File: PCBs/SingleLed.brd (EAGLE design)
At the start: 14.5 x 42 mm, 4 parts

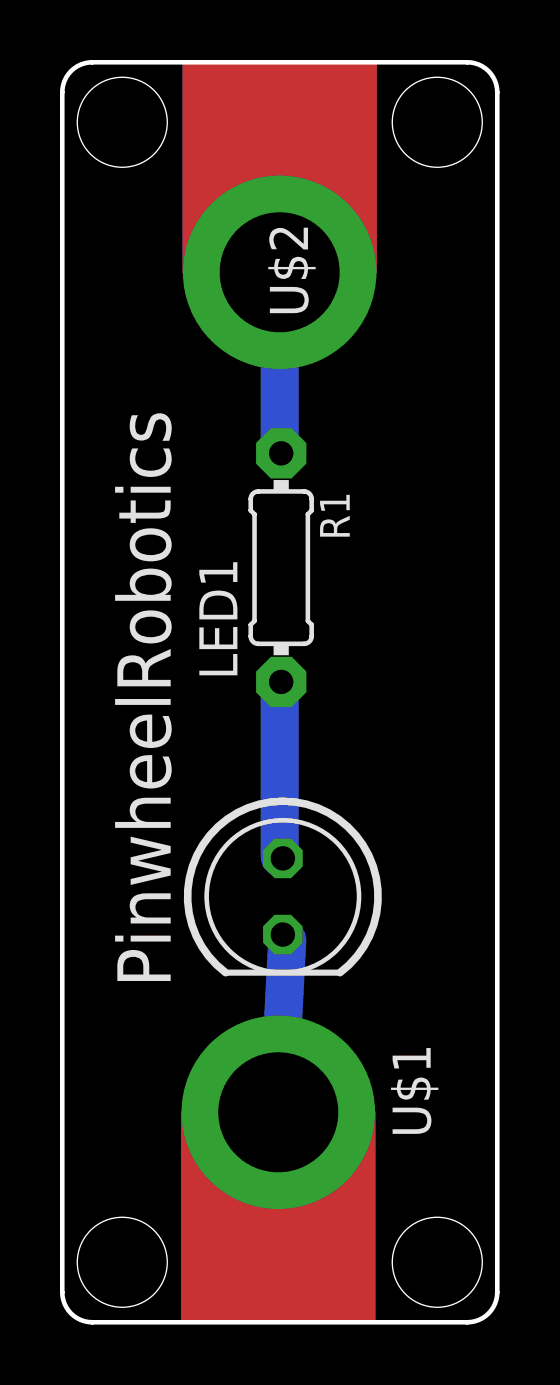
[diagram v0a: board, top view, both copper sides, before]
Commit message: Corrected dimesnion for
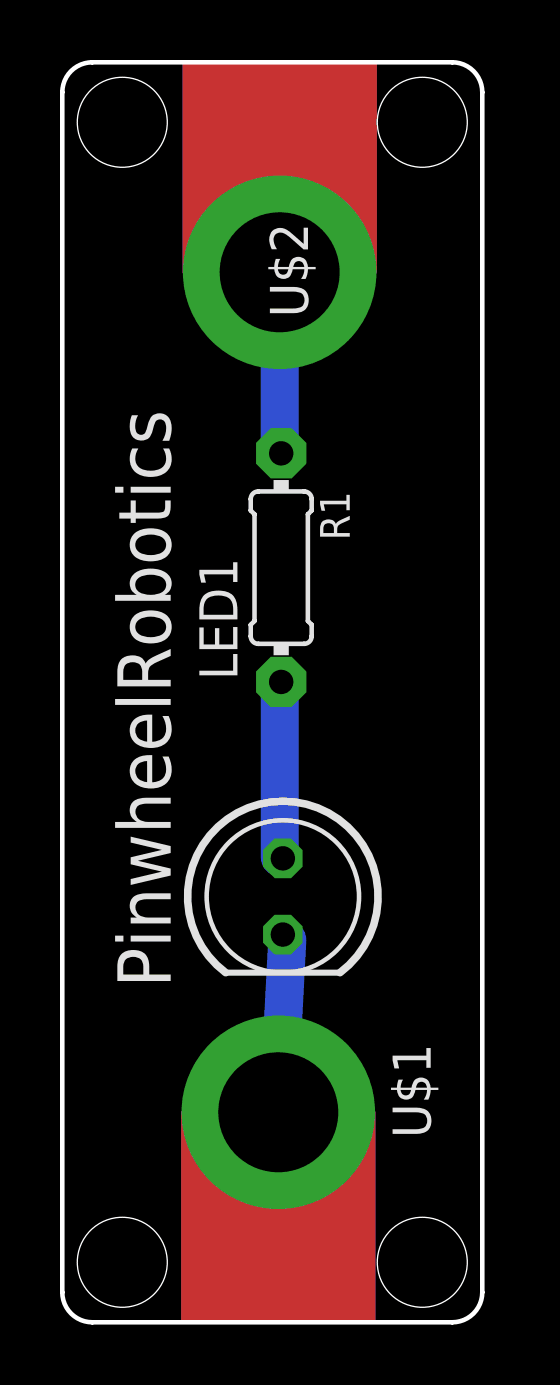
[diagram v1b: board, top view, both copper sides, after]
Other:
- board size 14.5 x 42 mm -> 14 x 42 mm
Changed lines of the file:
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@@
 <hole x="2" y="40" drill="3"/>
 <hole x="2" y="2" drill="3"/>
-<hole x="12.5" y="2" drill="3"/>
-<hole x="12.5" y="40" drill="3"/>
+<hole x="12" y="2" drill="3"/>
+<hole x="12" y="40" drill="3"/>
 <text x="3.613" y="11.161" size="1.778" layer="21" rot="R90">PinwheelRobotics</text>
 <text x="13.242" y="30.965" size="1.778" layer="22" rot="MR270">care@pinwheel.in</text>
-<wire x1="1" y1="0" x2="13.5" y2="0" width="0.1524" layer="20"/>
-<wire x1="13.5" y1="0" x2="14.5" y2="1" width="0.1524" layer="20" curve="90"/>
-<wire x1="14.5" y1="1" x2="14.5" y2="41" width="0.1524" layer="20"/>
-<wire x1="14.5" y1="41" x2="13.5" y2="42" width="0.1524" layer="20" curve="90"/>
-<wire x1="13.5" y1="42" x2="1" y2="42" width="0.1524" layer="20"/>
+<wire x1="1" y1="0" x2="13" y2="0" width="0.1524" layer="20"/>
+<wire x1="13" y1="0" x2="14" y2="1" width="0.1524" layer="20" curve="90"/>
+<wire x1="14" y1="1" x2="14" y2="41" width="0.1524" layer="20"/>
+<wire x1="14" y1="41" x2="13" y2="42" width="0.1524" layer="20" curve="90"/>
+<wire x1="13" y1="42" x2="1" y2="42" width="0.1524" layer="20"/>
 <wire x1="1" y1="42" x2="0" y2="41" width="0.1524" layer="20" curve="90"/>
 <wire x1="0" y1="41" x2="0" y2="1" width="0.1524" layer="20"/>
 <wire x1="0" y1="1" x2="1" y2="0" width="0.1524" layer="20" curve="90"/>
 <dimension x1="-2" y1="42" x2="-2" y2="0" x3="-3" y3="21" textsize="1.778" layer="1"/>
-<dimension x1="0" y1="42.5" x2="14.5" y2="42.5" x3="7.25" y3="44" textsize="1.778" layer="1"/>
+<dimension x1="13.5" y1="40" x2="13.5" y2="2" x3="20.5" y3="21" textsize="1.778" layer="1" dtype="diameter"/>
+<dimension x1="0" y1="43.5" x2="14" y2="43.5" x3="7" y3="45" textsize="1.778" layer="1"/>
+<dimension x1="2" y1="37.5" x2="12" y2="37.5" x3="7" y3="48.5" textsize="1.778" layer="1"/>
 </plain>
 <attributes>

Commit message: Update for Dim width is 42 length is 28 for type 2 pcb
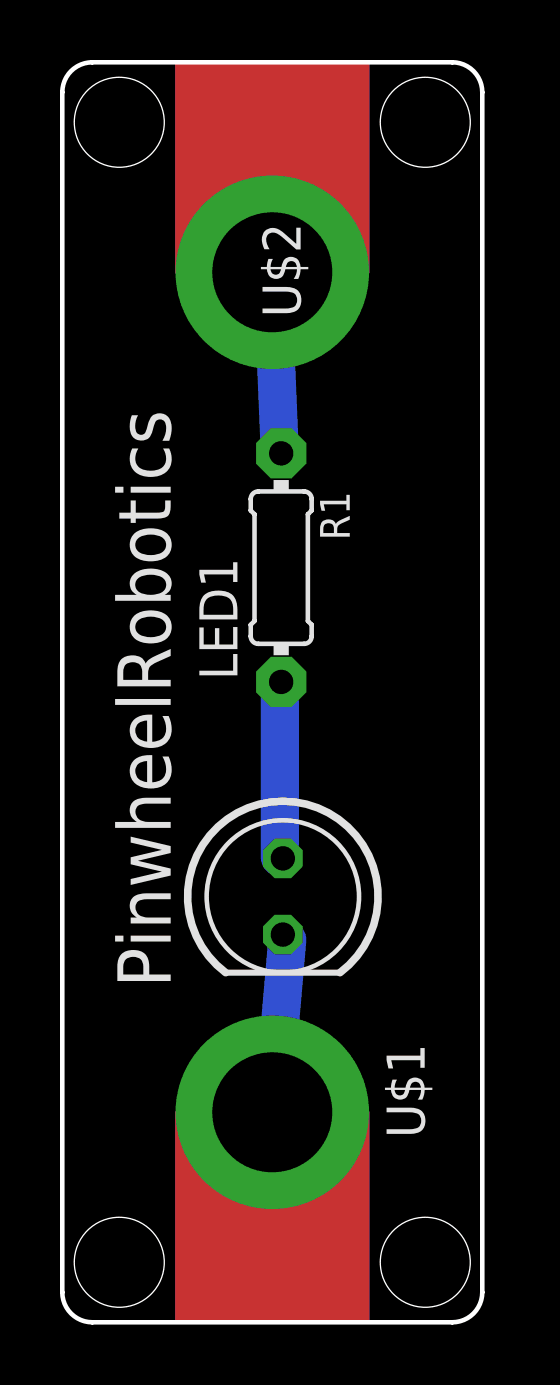
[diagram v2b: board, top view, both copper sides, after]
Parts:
- moved U$2 0.25 mm to (7.00, 35.0)
- moved U$1 0.20 mm to (7.00, 7.00)
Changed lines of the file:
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@@
 <drawing>
 <settings>
-<setting alwaysvectorfont="no"/>
+<setting alwaysvectorfont="yes"/>
 <setting verticaltext="up"/>
 </settings>
@@
 <board>
 <plain>
-<hole x="2" y="40" drill="3"/>
-<hole x="2" y="2" drill="3"/>
-<hole x="12" y="2" drill="3"/>
-<hole x="12" y="40" drill="3"/>
+<hole x="1.9" y="40" drill="3"/>
+<hole x="1.9" y="2" drill="3"/>
+<hole x="12.1" y="2" drill="3"/>
+<hole x="12.1" y="40" drill="3"/>
 <text x="3.613" y="11.161" size="1.778" layer="21" rot="R90">PinwheelRobotics</text>
 <text x="13.242" y="30.965" size="1.778" layer="22" rot="MR270">care@pinwheel.in</text>
@@
 <attribute name="VALUE" x="5.5486" y="10.9936" size="1.27" layer="27" ratio="10" rot="R270"/>
 </element>
-<element name="U$1" library="microbit" package="MICROBIT_PAD" value="MICROBIT_PAD" x="7.2" y="7" smashed="yes">
-<attribute name="NAME" x="11.01" y="9.286" size="1.27" layer="21" rot="R270"/>
+<element name="U$1" library="microbit" package="MICROBIT_PAD" value="MICROBIT_PAD" x="7" y="7" smashed="yes">
+<attribute name="NAME" x="10.81" y="9.286" size="1.27" layer="21" rot="R270"/>
 </element>
-<element name="U$2" library="microbit" package="MICROBIT_PAD" value="MICROBIT_PAD" x="7.246" y="35" smashed="yes" rot="R180">
-<attribute name="NAME" x="6.92" y="36.643" size="1.27" layer="21" rot="R270"/>
+<element name="U$2" library="microbit" package="MICROBIT_PAD" value="MICROBIT_PAD" x="7" y="35" smashed="yes" rot="R180">
+<attribute name="NAME" x="6.674" y="36.643" size="1.27" layer="21" rot="R270"/>
 </element>
 <element name="R1" library="adafruit" package="0204/7" value="" x="7.297" y="25.155" smashed="yes" rot="R270">
@@
 <contactref element="U$1" pad="PAD"/>
 <contactref element="LED1" pad="K"/>
-<wire x1="7.2" y1="7" x2="7.5" y2="12.75" width="1.27" layer="16"/>
+<wire x1="7" y1="7" x2="7.5" y2="12.75" width="1.27" layer="16"/>
 <wire x1="7.5" y1="12.75" x2="7.352" y2="12.924" width="0.1524" layer="16"/>
 </signal>
@@
 <contactref element="U$2" pad="PAD"/>
 <contactref element="R1" pad="1"/>
-<wire x1="7.246" y1="35" x2="7.246" y2="29.083575" width="1.27" layer="16"/>
+<wire x1="7" y1="35" x2="7.246" y2="29.083575" width="1.27" layer="16"/>
 <wire x1="7.246" y1="29.083575" x2="7.297" y2="28.965" width="0.1524" layer="16"/>
 </signal>

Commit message: Corrected hole position for some design , made transistor as switch as category 1
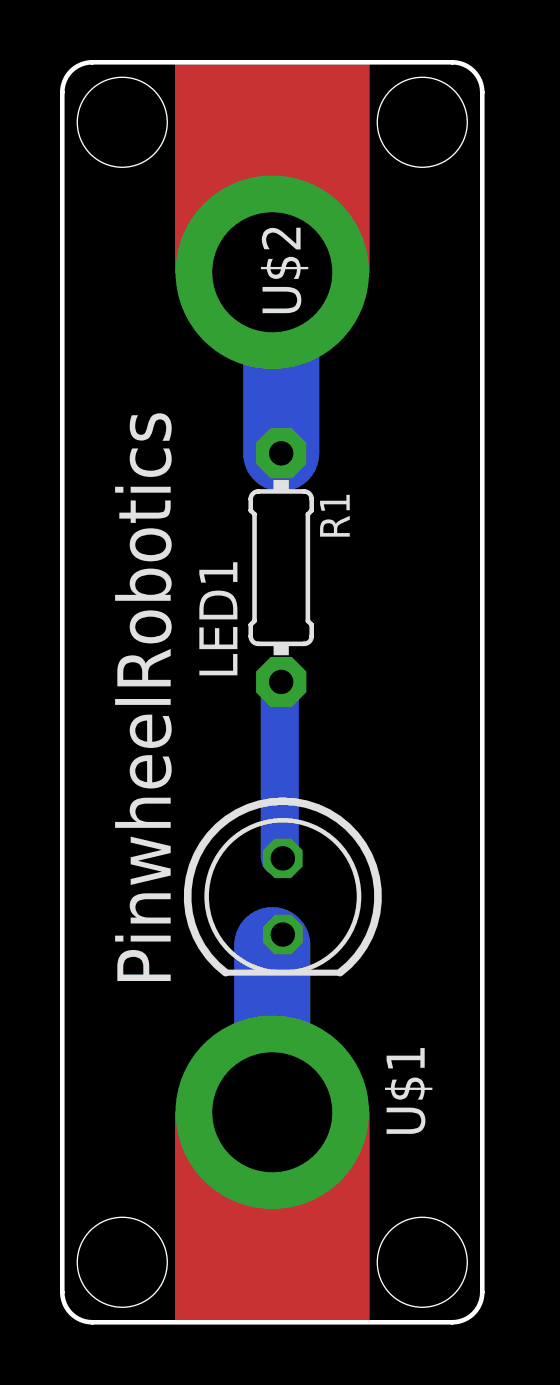
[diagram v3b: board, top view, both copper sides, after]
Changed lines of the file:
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@@
 <drawing>
 <settings>
-<setting alwaysvectorfont="yes"/>
+<setting alwaysvectorfont="no"/>
 <setting verticaltext="up"/>
 </settings>
@@
 <board>
 <plain>
-<hole x="1.9" y="40" drill="3"/>
-<hole x="1.9" y="2" drill="3"/>
-<hole x="12.1" y="2" drill="3"/>
-<hole x="12.1" y="40" drill="3"/>
+<hole x="2" y="40" drill="3"/>
+<hole x="2" y="2" drill="3"/>
+<hole x="12" y="2" drill="3"/>
+<hole x="12" y="40" drill="3"/>
 <text x="3.613" y="11.161" size="1.778" layer="21" rot="R90">PinwheelRobotics</text>
 <text x="13.242" y="30.965" size="1.778" layer="22" rot="MR270">care@pinwheel.in</text>
@@
 <contactref element="U$1" pad="PAD"/>
 <contactref element="LED1" pad="K"/>
-<wire x1="7" y1="7" x2="7.5" y2="12.75" width="1.27" layer="16"/>
-<wire x1="7.5" y1="12.75" x2="7.352" y2="12.924" width="0.1524" layer="16"/>
+<wire x1="7.352" y1="12.924" x2="7" y2="12.572" width="1.27" layer="16"/>
+<wire x1="7" y1="7" x2="7" y2="12.572" width="2.54" layer="16"/>
 </signal>
 <signal name="N$1">
@@
 <contactref element="U$2" pad="PAD"/>
 <contactref element="R1" pad="1"/>
-<wire x1="7" y1="35" x2="7.246" y2="29.083575" width="1.27" layer="16"/>
-<wire x1="7.246" y1="29.083575" x2="7.297" y2="28.965" width="0.1524" layer="16"/>
+<wire x1="7.297" y1="28.965" x2="7.297" y2="34.703" width="2.54" layer="16"/>
+<wire x1="7" y1="35" x2="7.297" y2="34.703" width="1.27" layer="16"/>
 </signal>
 </signals>
